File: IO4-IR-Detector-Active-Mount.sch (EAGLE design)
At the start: 2 parts

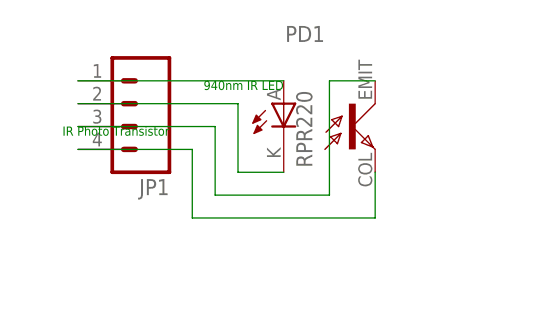
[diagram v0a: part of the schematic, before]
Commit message: added values for connectors
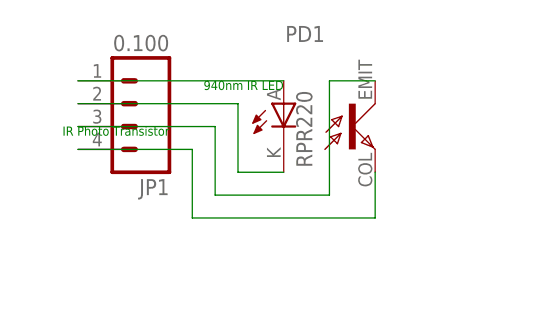
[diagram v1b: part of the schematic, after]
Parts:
- JP1: value (none) -> 0.100
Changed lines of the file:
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@@
 </classes>
 <parts>
-<part name="JP1" library="SPCoast" deviceset="CONNECTOR-M04" device="LOCK"/>
+<part name="JP1" library="SPCoast" deviceset="CONNECTOR-M04" device="LOCK" value="0.100"/>
 <part name="FRAME1" library="SPCoast" deviceset="DOC-FRAME-LETTER" device=""/>
 <part name="PD1" library="SPCoast" deviceset="PHOTODETECTOR" device="" value="RPR220"/>
